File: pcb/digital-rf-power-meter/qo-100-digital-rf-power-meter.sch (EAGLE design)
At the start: 40 parts, among them CON1 4P-SH-SIDE, U1 F2915NBGK, U2 ADP7142AUJZ-3.3, U3 MCP23008

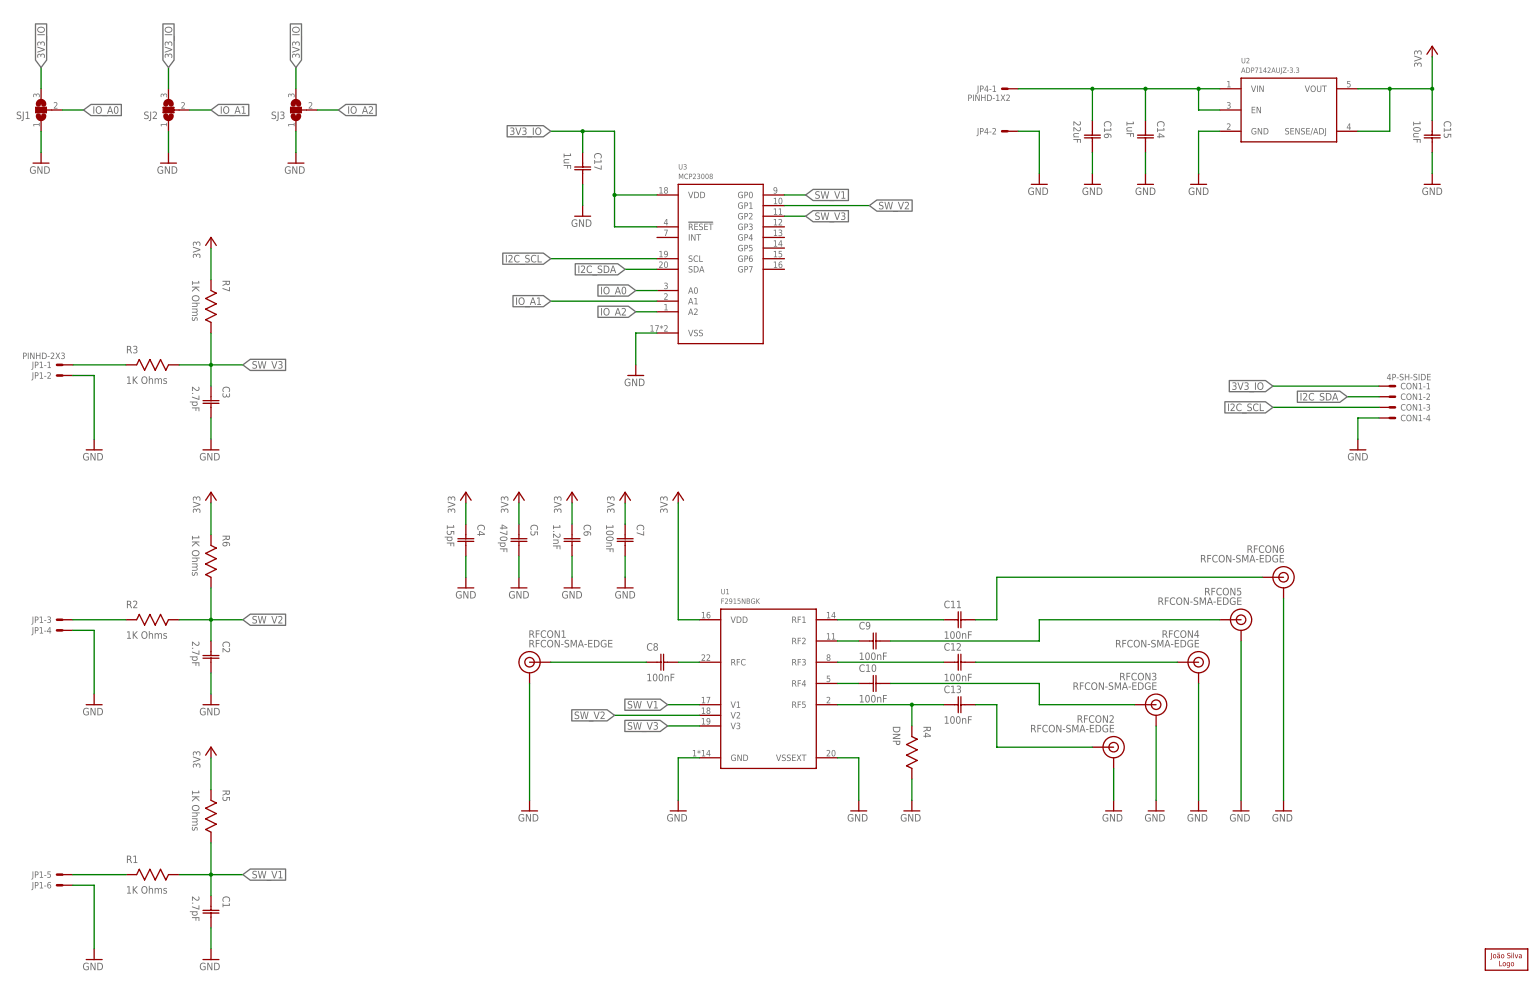
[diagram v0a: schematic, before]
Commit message: Renamed RF Power meter Added Power meter Added IO expander to RF switch PCB to make it work thru I2C
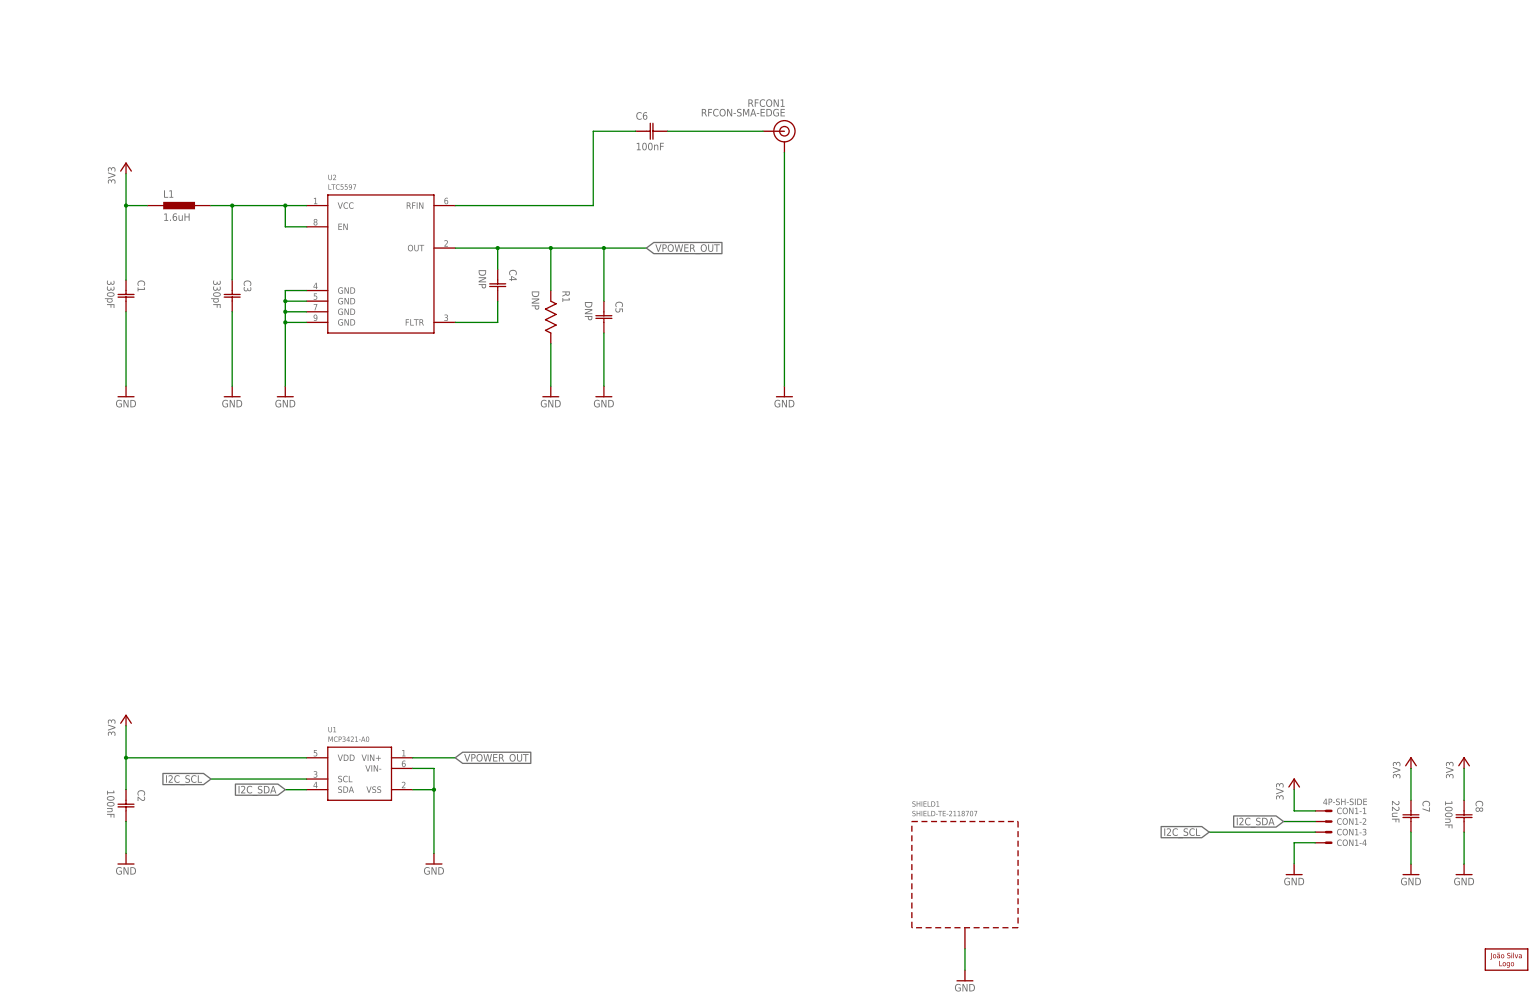
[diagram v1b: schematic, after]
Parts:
- removed C10, C11, C12, C13, C9: 100nF, Capacitor:CAPACITOR-0603
- removed C14, C17: 1uF, Capacitor:CAPACITOR-0603
- removed C15: 10uF, Capacitor:CAPACITOR-0603
- removed C16: 22uF, Capacitor:CAPACITOR-1206
- removed JP1: PINHD-2X3, Pin Header:PINHD-2X3
- removed JP4: PINHD-1X2, Pin Header:PINHD-1X2
- removed R2, R3, R5, R6, R7: 1K Ohms, Resistor:RESISTOR-0603
- removed R4: DNP, Resistor:RESISTOR-0603
- removed RFCON2, RFCON3, RFCON4, RFCON5, RFCON6: RFCON-SMA-EDGE, RF Connector:RFCON-SMA-EDGE
- removed SJ1, SJ2, SJ3: (no value), Solder Jumper:SJ2S
- removed U3: MCP23008, Microchip:MCP23008
- added L1: 1.6uH, Inductor:INDUCTOR-0603
- added SHIELD1: SHIELD-TE-2118707, Shield:SHIELD-TE-2118707
- C1, C3: value 2.7pF -> 330pF
- C2: value 2.7pF -> 100nF
- C4: value 15pF -> DNP
- C5: value 470pF -> DNP
- C6: value 1.2nF -> 100nF
- C7: value 100nF -> 22uF; device Capacitor:CAPACITOR-0603 -> Capacitor:CAPACITOR-1206
- R1: value 1K Ohms -> DNP
- U1: value F2915NBGK -> MCP3421-A0; device Renesas:F2915NBGK -> Microchip:MCP3421-A0
- U2: value ADP7142AUJZ-3.3 -> LTC5597; device Analog Devices:ADP7142AUJZ-3.3 -> Analog Devices:LTC5597
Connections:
- removed net 3V3_IO: C17.C1, CON1-1.S, SJ1.3, SJ2.3, SJ3.3, U3.!RESET, U3.VDD
- removed net IO_A0: SJ1.2, U3.A0
- removed net IO_A1: SJ2.2, U3.A1
- removed net IO_A2: SJ3.2, U3.A2
- removed net N$10: C12.C2, RFCON4.SIGNAL
- removed net N$11: C9.C2, RFCON5.SIGNAL
- removed net N$12: C11.C2, RFCON6.SIGNAL
- removed net N$13: JP1-1.S, R3.2
- removed net N$14: JP1-3.S, R2.2
- removed net N$15: JP1-5.S, R1.2
- removed net N$16: C14.C1, C16.C1, JP4-1.S, U2.EN, U2.VIN
- removed net N$5: C12.C1, U1.RF3
- removed net N$6: C9.C1, U1.RF2
- removed net N$7: C11.C1, U1.RF1
- removed net N$8: C13.C2, RFCON2.SIGNAL
- removed net N$9: C10.C2, RFCON3.SIGNAL
- removed net SW_V1: C1.C1, R1.1, R5.1, U1.V1, U3.GP0
- removed net SW_V2: C2.C1, R2.1, R6.1, U1.V2, U3.GP1
- removed net SW_V3: C3.C1, R3.1, R7.1, U1.V3, U3.GP2
- new net VPOWER_OUT: C4.C1, C5.C1, R1.2, U1.VIN+, U2.OUT
- net 3V3: now also C1.C1, C2.C1, C8.C1, CON1-1.S, L1.1; no longer C15.C1, C4.C1, C5.C1, C6.C1, R5.2, R6.2, R7.2, U2.SENSE/ADJ, U2.VOUT
- net GND: now also C8.C2, R1.1, SHIELD1.GND, U1.VIN-, U1.VSS, U2.GND@0, U2.GND@1, U2.GND@2, U2.GND@3; no longer C14.C2, C15.C2, C16.C2, C17.C2, C4.C2, C6.C2, JP1-2.S, JP1-4.S, JP1-6.S, JP4-2.S, R4.1, RFCON2.GND, RFCON3.GND, RFCON4.GND, RFCON5.GND, RFCON6.GND, SJ1.1, SJ2.1, SJ3.1, U1.GND, U1.VSSEXT, U2.GND, U3.VSS
- net I2C_SCL: now also U1.SCL; no longer U3.SCL
- net I2C_SDA: now also U1.SDA; no longer U3.SDA
- net N$1: now also C6.C1, U2.RFIN; no longer C8.C1, RFCON1.SIGNAL
- net N$2: now also C6.C2, RFCON1.SIGNAL; no longer C8.C2, U1.RFC
- net N$3: now also C4.C2, U2.FLTR; no longer C13.C1, R4.2, U1.RF5
- net N$4: now also C3.C1, L1.2, U2.EN, U2.VCC; no longer C10.C1, U1.RF4
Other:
- note removed: "Install R4 for F2914 Do not install R4 for F2915"
- moved on the sheet: C1, C2, C3, C4, C5, C6, C7, C8, CON1-1, CON1-2, CON1-3, CON1-4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

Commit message: Add Ripple blocker to RF power meter
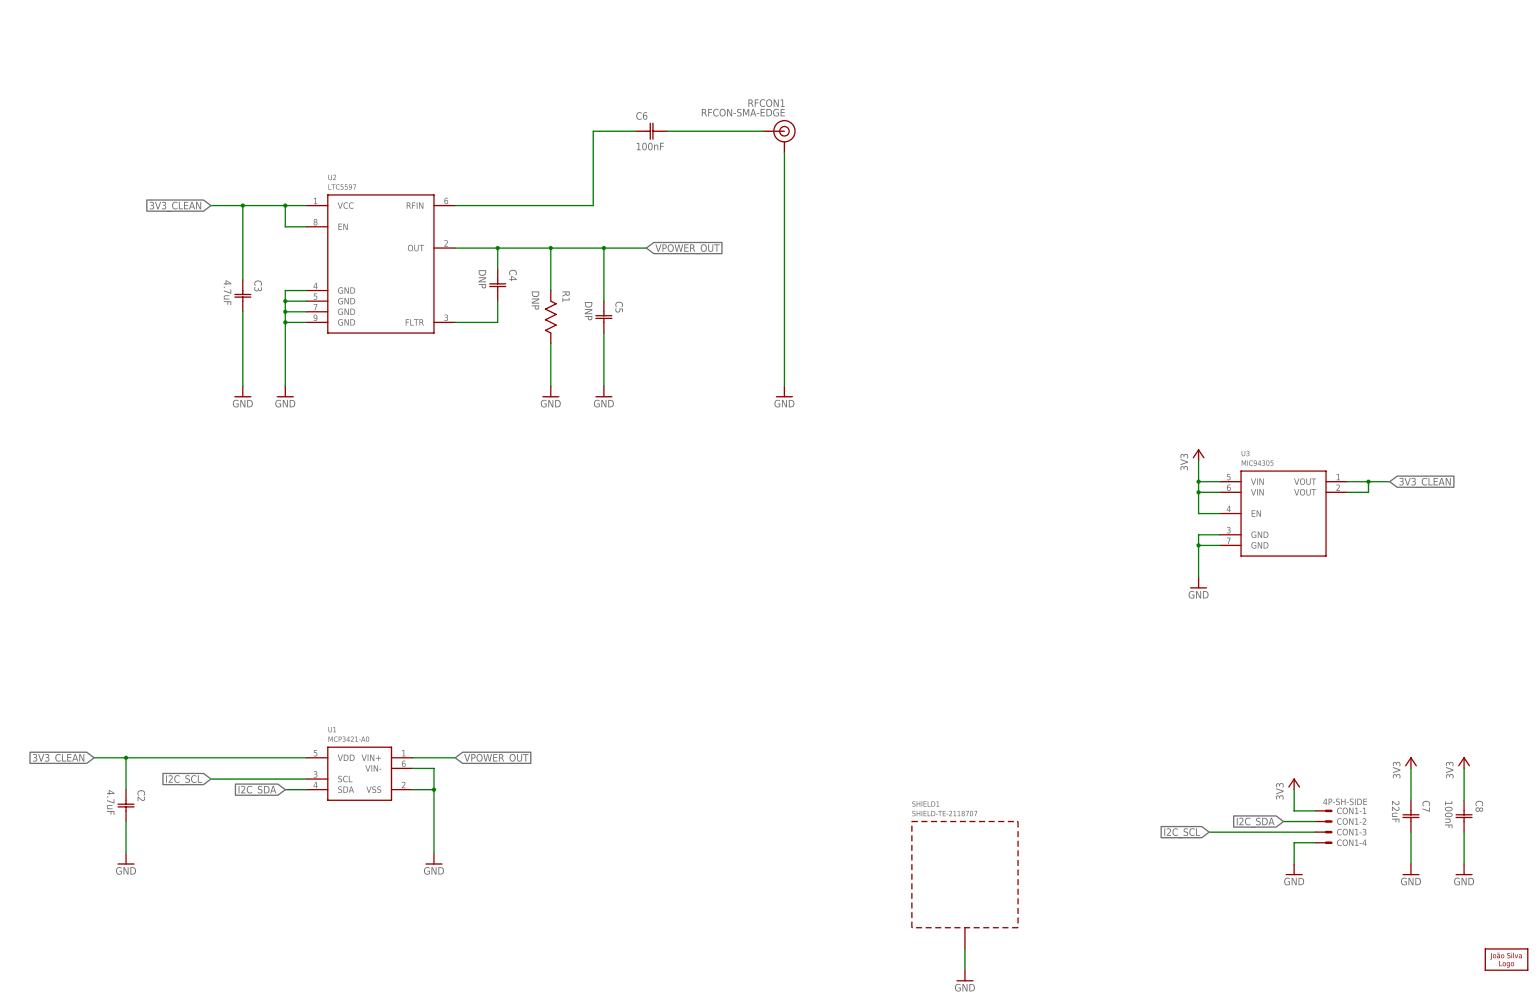
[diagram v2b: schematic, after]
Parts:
- removed C1: 330pF, Capacitor:CAPACITOR-0603
- removed L1: 1.6uH, Inductor:INDUCTOR-0603
- added U3: MIC94305, Microchip:MIC94305
- C2: value 100nF -> 4.7uF
- C3: value 330pF -> 4.7uF
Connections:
- removed net N$4: C3.C1, L1.2, U2.EN, U2.VCC
- new net 3V3_CLEAN: C2.C1, C3.C1, U1.VDD, U2.EN, U2.VCC, U3.VOUT@0, U3.VOUT@1
- net 3V3: now also U3.EN, U3.VIN@0, U3.VIN@1; no longer C1.C1, C2.C1, L1.1, U1.VDD
- net GND: now also U3.GND@0, U3.GND@1; no longer C1.C2
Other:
- moved on the sheet: C3

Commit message: Work on PCBs
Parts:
- C4: value DNP -> 10nF
- C5: value DNP -> 1uF
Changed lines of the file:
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@@
 <part name="C3" library="Capacitor" deviceset="CAPACITOR" device="-0603" value="4.7uF"/>
 <part name="GND4" library="Supply Symbol" deviceset="GND" device=""/>
-<part name="C4" library="Capacitor" deviceset="CAPACITOR" device="-0603" value="DNP"/>
-<part name="C5" library="Capacitor" deviceset="CAPACITOR" device="-0603" value="DNP"/>
+<part name="C4" library="Capacitor" deviceset="CAPACITOR" device="-0603" value="10nF"/>
+<part name="C5" library="Capacitor" deviceset="CAPACITOR" device="-0603" value="1uF"/>
 <part name="GND7" library="Supply Symbol" deviceset="GND" device=""/>
 <part name="GND8" library="Supply Symbol" deviceset="GND" device=""/>
